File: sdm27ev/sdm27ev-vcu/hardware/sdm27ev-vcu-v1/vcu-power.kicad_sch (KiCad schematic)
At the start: 40 parts, among them IC1 TPD4E05U06QDQARQ1, IC2 TPS2121RUXR, IC3 TPS56637RPAR, IC4 TPS61023DRLT, J5 USB4725-03-C-KIT, Q1 RRL035P03FRATR, U3 HUSB238

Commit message: Minor QOL VCU edits before design review
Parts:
- added C72: 10uF, Capacitor_SMD:C_0603_1608Metric, symbol Device:C_Small
- added C73: 100nF, Capacitor_SMD:C_0603_1608Metric, symbol Device:C_Small
- added FB1: 600 Ohm 100mhz, Inductor_SMD:L_0603_1608Metric, symbol Device:FerriteBead_Small
- R32: value 20k -> 47k
- R35: now fitted
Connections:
- net 5VA: now also C72.1, C73.1, FB1.2; no longer C20.1, IC4.6 (VOUT), R12.1
- net GND: now also C72.2, C73.2
- new net: C20.1, FB1.1, IC4.6 (VOUT), R12.1
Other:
- note added: "Current limit 2.37A"
- note removed: "Current limit 1.24A"

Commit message: notes from ev vcu design review 10 3
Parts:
- added R11, R79: 5.1k, Resistor_SMD:R_0603_1608Metric, symbol Device:R_Small
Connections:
- net GND: now also R11.2, R79.2
- net at IC1.4 (D2+), J5.A5 (CC1), U3.4 (CC1): now also R79.1
- net at IC1.5 (D2-), J5.B5 (CC2), U3.5 (CC2): now also R11.1

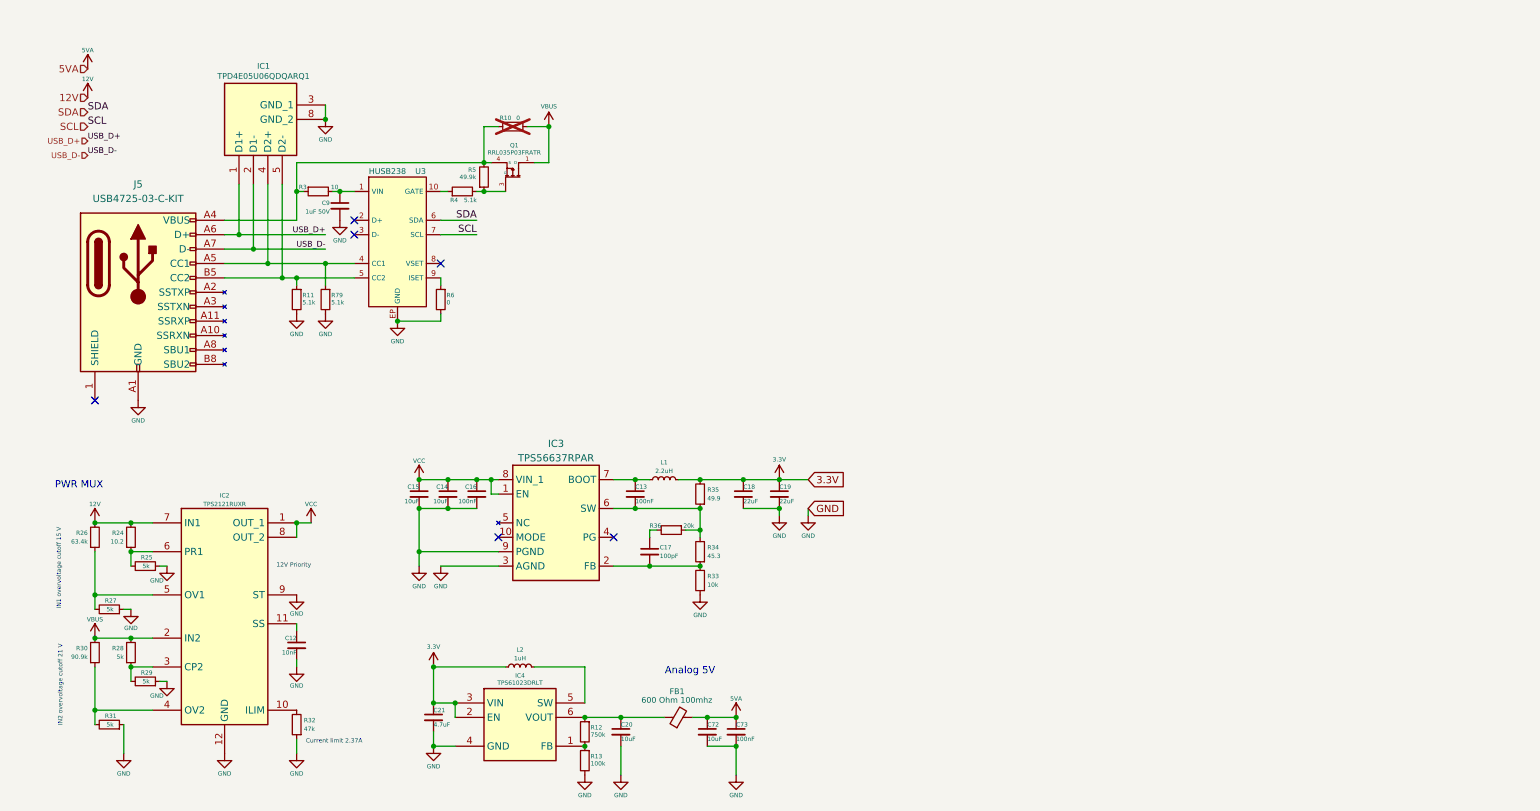
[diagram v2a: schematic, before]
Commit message: VCU sch reorg and power rework
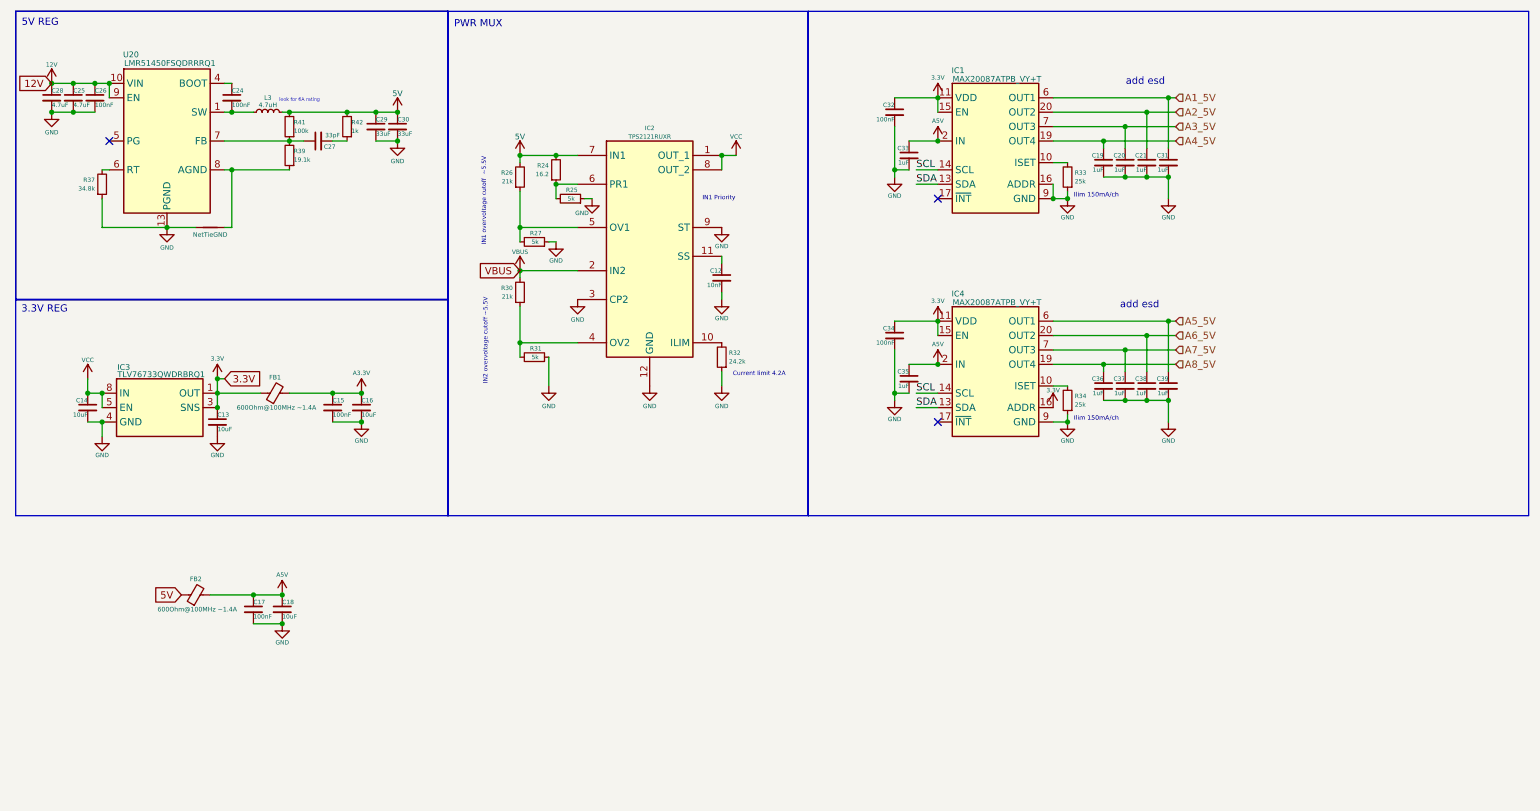
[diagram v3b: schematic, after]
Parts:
- removed C72: 10uF, Capacitor_SMD:C_0603_1608Metric, symbol Device:C_Small
- removed C73: 100nF, Capacitor_SMD:C_0603_1608Metric, symbol Device:C_Small
- removed C9: 1uF 50V, Capacitor_SMD:C_0603_1608Metric, symbol Device:C_Small
- removed IC1: TPD4E05U06QDQARQ1, DQA(R-PUSON-N10), symbol SDM_EV:TPD4E05U06QDQARQ1
- removed IC3: TPS56637RPAR, TPS56637RPAR, symbol SDM_EV:TPS56637RPAR
- removed IC4: TPS61023DRLT, SOTFL50P160X60-6N, symbol SDM_EV:TPS61023DRLT
- removed J5: USB4725-03-C-KIT, SDM_Misc:GCT_USB4730-GF-A_REVA, symbol SDM_MISC:USB4725-03-C-KIT
- removed L1: 2.2uH, Inductor_SMD:L_7.3x7.3_H3.5, symbol Device:L_Small
- removed L2: 1uH, Inductor_SMD:L_Changjiang_FTC404010S, symbol Device:L_Small
- removed Q1: RRL035P03FRATR, RRL035P03FRATR, symbol SDM_EV:RRL035P03FRATR
- removed R10, R6: 0, Resistor_SMD:R_0603_1608Metric, symbol Device:R_Small
- removed R11, R4, R79: 5.1k, Resistor_SMD:R_0603_1608Metric, symbol Device:R_Small
- removed R12: 750k, Resistor_SMD:R_0603_1608Metric, symbol Device:R_Small
- removed R13: 100k, Resistor_SMD:R_0603_1608Metric, symbol Device:R_Small
- removed R28, R29: 5k, Resistor_SMD:R_0402_1005Metric, symbol Device:R_Small
- removed R3: 10, Resistor_SMD:R_0603_1608Metric, symbol Device:R_Small
- removed R35: 49.9, Resistor_SMD:R_0402_1005Metric, symbol Device:R_Small
- removed R36: 20k, Resistor_SMD:R_0402_1005Metric, symbol Device:R_Small
- removed R5: 49.9k, Resistor_SMD:R_0603_1608Metric, symbol Device:R_Small
- removed U3: HUSB238, symbol SDM_EV:HUSB238
- added C24, C26, C32, C34: 100nF, Capacitor_SMD:C_0603_1608Metric, symbol Device:C_Small
- added C25, C28: 4.7uF, Capacitor_SMD:C_0805_2012Metric, symbol Device:C_Small
- added C27: 33pF, Capacitor_SMD:C_0603_1608Metric, symbol Device:C_Small
- added C29, C30: 33uF, Capacitor_SMD:C_0805_2012Metric, symbol Device:C_Small
- added C31, C33, C35, C36, C37, C38, C39: 1uF, Capacitor_SMD:C_0603_1608Metric, symbol Device:C_Small
- added FB2: 600Ohm@100MHz ~1.4A, Inductor_SMD:L_0805_2012Metric, symbol Device:FerriteBead_Small
- added IC1, IC4: MAX20087ATPB_VY+T, QFN50P400X400X80-21N-D, symbol SDM_EV:MAX20087ATPB_VY+T
- added IC3: TLV76733QWDRBRQ1, SON65P300X300X100-9N-D, symbol SDM_EV:TLV76733QWDRBRQ1
- added L3: 4.7uH, Inductor_SMD:L_SXN_SMDRI62, symbol Device:L_Small
- added NT1: NetTieGND, symbol Device:NetTie_2
- added R37: 34.8k, Resistor_SMD:R_0402_1005Metric, symbol Device:R_Small
- added R39: 19.1k, Resistor_SMD:R_0402_1005Metric, symbol Device:R_Small
- added R41: 100k, Resistor_SMD:R_0402_1005Metric, symbol Device:R_Small
- added R42: 1k, Resistor_SMD:R_0402_1005Metric, symbol Device:R_Small
- added U20: LMR51450FSQDRRRQ1, SON50P300X300X80-13N-D, symbol SDM_EV:LMR51450FSQDRRRQ1
- C13, C16: value 100nF -> 10uF; footprint Capacitor_SMD:C_0603_1608Metric -> Capacitor_SMD:C_0805_2012Metric
- C14: footprint Capacitor_SMD:C_0603_1608Metric -> Capacitor_SMD:C_0805_2012Metric
- C15: value 10uF -> 100nF
- C17: value 100pF -> 100nF
- C18: value 22uF -> 10uF; footprint Capacitor_SMD:C_0603_1608Metric -> Capacitor_SMD:C_0805_2012Metric
- C19: value 22uF -> 1uF
- C20: value 10uF -> 1uF
- C21: value 4.7uF -> 1uF
- FB1: value 600 Ohm 100mhz -> 600Ohm@100MHz ~1.4A; footprint Inductor_SMD:L_0603_1608Metric -> Inductor_SMD:L_0805_2012Metric
- R24: value 10.2 -> 16.2
- R26: value 63.4k -> 21k
- R30: value 90.9k -> 21k
- R32: value 47k -> 24.2k
- R33: value 10k -> 25k
- R34: value 45.3 -> 25k
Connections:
- net 12V: now also C25.1, C26.1, C28.1, U20.10 (VIN), U20.11 (VIN_2), U20.12 (VIN_3), U20.9 (EN); no longer IC2.7 (IN1), R24.2, R26.2
- net 3.3V: now also C13.1, FB1.1, C32.1, C34.1, IC1.11 (VDD), IC1.15 (EN), IC3.1 (OUT), IC3.3 (SNS), IC4.11 (VDD), IC4.15 (EN), IC4.16 (ADDR); no longer C18.1, C19.1, C21.1
- net GND: now also C13.2, C17.2, IC2.3 (CP2), R34.1, C25.2, C26.2, C28.2, C29.2, C30.2, C31.2, C32.2, C33.2, C34.2, C35.2, C36.2, C37.2, C38.2, C39.2, IC1.1 (PGND_1), IC1.12 (GND_2), IC1.16 (ADDR), IC1.21 (EP), IC1.5 (PGND_2), IC1.9 (GND), IC3.4 (GND), IC3.6 (GND_2), IC3.9 (EP), IC4.1 (PGND_1), IC4.12 (GND_2), IC4.21 (EP), IC4.5 (PGND_2), IC4.9 (GND), NT1.1, R37.1, U20.13 (PGND)
- net SCL: now also IC1.14 (SCL), IC4.14 (SCL)
- net SDA: now also IC1.13 (SDA), IC4.13 (SDA)
- net VCC: now also IC3.5 (EN), IC3.8 (IN); no longer C15.1, C16.1
- net A3_5V: now reaches C20.1
- net A3_5V: now also IC1.7 (OUT3); no longer FB1.1
- net at R34.2: now also IC4.10 (ISET); no longer C13.2
- net A5V: now reaches C17.1
- net A5V: now also C18.1, C33.1, C35.1, FB2.2, IC1.2 (IN), IC1.3 (IN_2), IC1.4 (IN_3), IC4.2 (IN), IC4.3 (IN_2), IC4.4 (IN_3)
- net 5VA renamed A3.3V
- net A3.3V: now also C15.1, C16.1
- new net: NT1.2, R39.1, U20.8 (AGND)
- new net: C27.1, R39.2, R41.1, U20.7 (FB)
- new net: C24.2, L3.1, U20.1 (SW), U20.2 (SW_2), U20.3 (SW_3)
- new net: C24.1, U20.4 (BOOT)
- new net: R37.2, U20.6 (RT)
- new net: IC1.10 (ISET), R33.2
- new net: C27.2, R42.1
- new net 5V: C29.1, C30.1, FB2.1, IC2.7 (IN1), L3.2, R24.2, R26.2, R41.2, R42.2
- new net A1_5V: C31.1, IC1.6 (OUT1)
- new net A2_5V: C21.1, IC1.20 (OUT2)
- new net A4_5V: C19.1, IC1.19 (OUT4)
- new net A5_5V: C39.1, IC4.6 (OUT1)
- new net A6_5V: C38.1, IC4.20 (OUT2)
- new net A7_5V: C37.1, IC4.7 (OUT3)
- new net A8_5V: C36.1, IC4.19 (OUT4)
- no-connect marks 6 -> 3
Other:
- note added: "3.3V REG"
- note added: "5V REG"
- note added: "Current limit 4.2A"
- note added: "IN1 Priority"
- note added: "IN1 overvoltage cutoff ~5.5V"
- note added: "IN2 overvoltage cutoff ~5.5V"
- note added: "Ilim 150mA/ch"
- note added: "add esd"
- note added: "look for 6A rating"
- note removed: "12V Priority"
- note removed: "Analog 5V"
- note removed: "Current limit 2.37A"
- note removed: "IN1 overvoltage cutoff 15 V"
- note removed: "IN2 overvoltage cutoff 21 V"
- moved on the sheet: C12, IC2, R24, R25, R26, R27, R30, R31, R32

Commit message: EV VCU edits, mostly organizational and pre layout/footprint assigned
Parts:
- IC1, IC4: footprint QFN50P400X400X80-21N-D -> SDM_EV:QFN50P400X400X80-21N-D
- IC3: footprint SON65P300X300X100-9N-D -> (none)
- R24, R25, R26, R27, R30, R31, R32, R33, R34, R37, R39, R41, R42: footprint Resistor_SMD:R_0402_1005Metric -> Resistor_SMD:R_0603_1608Metric
- U20: footprint SON50P300X300X80-13N-D -> SDM_EV:SON50P300X300X80-13N-D
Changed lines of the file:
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@@
 	)
 	(junction
-		(at 73.66 80.01)
-		(diameter 0)
-		(color 0 0 0 0)
-	)
-	(junction
 		(at 175.26 74.93)
 		(diameter 0)
@@
 	)
 	(junction
+		(at 73.66 77.47)
+		(diameter 0)
+		(color 0 0 0 0)
+	)
+	(junction
 		(at 167.64 40.64)
 		(diameter 0)
@@
 	)
 	(junction
+		(at 73.66 80.01)
+		(diameter 0)
+		(color 0 0 0 0)
+	)
+	(junction
 		(at 39.37 50.8)
 		(diameter 0)
@@
 	(wire
 		(pts
+			(xy 73.66 77.47) (xy 74.93 77.47)
+		)
+		(stroke
+			(width 0)
+			(type default)
+		)
+	)
+	(wire
+		(pts
 			(xy 167.64 80.01) (xy 170.18 80.01)
 		)
@@
 	(wire
 		(pts
+			(xy 73.66 77.47) (xy 73.66 80.01)
+		)
+		(stroke
+			(width 0)
+			(type default)
+		)
+	)
+	(wire
+		(pts
 			(xy 19.05 30.48) (xy 22.86 30.48)
 		)
@@
 		)
 	)
+	(global_label "A3.3V"
+		(shape input)
+		(at 74.93 77.47 0)
+		(fields_autoplaced yes)
+		(effects
+			(font
+				(size 1.27 1.27)
+			)
+			(justify left)
+		)
+		(property "Intersheetrefs" "${INTERSHEET_REFS}"
+			(at 83.1162 77.47 0)
+			(hide yes)
+			(show_name no)
+			(do_not_autoplace no)
+			(effects
+				(font
+					(size 1.27 1.27)
+				)
+				(justify left)
+			)
+		)
+	)
 	(global_label "12V"
 		(shape input)
@@
 		)
 	)
+	(global_label "VCC"
+		(shape input)
+		(at 139.7 38.1 0)
+		(fields_autoplaced yes)
+		(effects
+			(font
+				(size 1.27 1.27)
+			)
+			(justify left)
+		)
+		(property "Intersheetrefs" "${INTERSHEET_REFS}"
+			(at 146.3138 38.1 0)
+			(hide yes)
+			(show_name no)
+			(do_not_autoplace no)
+			(effects
+				(font
+					(size 1.27 1.27)
+				)
+				(justify left)
+			)
+		)
+	)
 	(hierarchical_label "A8_5V"
 		(shape input)
@@
 			)
 		)
-		(property "Footprint" "SON65P300X300X100-9N-D"
+		(property "Footprint" ""
 			(at 52.07 174.93 0)
 			(hide yes)
@@
 			)
 		)
-		(property "Footprint" "Resistor_SMD:R_0402_1005Metric"
+		(property "Footprint" "Resistor_SMD:R_0603_1608Metric"
 			(at 137.16 73.66 0)
 			(hide yes)
@@
 			)
 		)
-		(property "Footprint" "Resistor_SMD:R_0402_1005Metric"
+		(property "Footprint" "Resistor_SMD:R_0603_1608Metric"
 			(at 60.96 38.1 0)
 			(hide yes)
@@
 			)
 		)
-		(property "Footprint" "SON50P300X300X80-13N-D"
+		(property "Footprint" "SDM_EV:SON50P300X300X80-13N-D"
 			(at 53.34 120.32 0)
 			(hide yes)
@@
 			)
 		)
-		(property "Footprint" "Resistor_SMD:R_0402_1005Metric"
+		(property "Footprint" "Resistor_SMD:R_0603_1608Metric"
 			(at 60.96 33.02 0)
 			(hide yes)
@@
 	(symbol
 		(lib_id "power:+3.3V")
-		(at 73.66 80.01 0)
+		(at 73.66 77.47 0)
 		(unit 1)
 		(body_style 1)
@@
 		(dnp no)
 		(property "Reference" "#PWR0161"
-			(at 73.66 83.82 0)
+			(at 73.66 81.28 0)
 			(hide yes)
 			(show_name no)
@@
 		)
 		(property "Value" "A3.3V"
-			(at 73.66 76.454 0)
+			(at 73.66 73.914 0)
 			(show_name no)
 			(do_not_autoplace no)
@@
 		)
 		(property "Footprint" ""
-			(at 73.66 80.01 0)
+			(at 73.66 77.47 0)
 			(hide yes)
 			(show_name no)
@@
 		)
 		(property "Datasheet" ""
-			(at 73.66 80.01 0)
+			(at 73.66 77.47 0)
 			(hide yes)
 			(show_name no)
@@
 		)
 		(property "Description" "Power symbol creates a global label with name \"+3.3V\""
-			(at 73.66 80.01 0)
+			(at 73.66 77.47 0)
 			(hide yes)
 			(show_name no)
@@
 			)
 		)
-		(property "Footprint" "Resistor_SMD:R_0402_1005Metric"
+		(property "Footprint" "Resistor_SMD:R_0603_1608Metric"
 			(at 198.12 41.91 0)
 			(hide yes)
@@
 			)
 		)
-		(property "Footprint" "Resistor_SMD:R_0402_1005Metric"
+		(property "Footprint" "Resistor_SMD:R_0603_1608Metric"
 			(at 104.14 53.34 0)
 			(hide yes)
@@
 			)
 		)
-		(property "Footprint" "Resistor_SMD:R_0402_1005Metric"
+		(property "Footprint" "Resistor_SMD:R_0603_1608Metric"
 			(at 104.14 73.66 0)
 			(hide yes)
@@
 			)
 		)
-		(property "Footprint" "Resistor_SMD:R_0402_1005Metric"
+		(property "Footprint" "Resistor_SMD:R_0603_1608Metric"
 			(at 198.12 81.28 0)
 			(hide yes)
@@
 			)
 		)
-		(property "Footprint" "QFN50P400X400X80-21N-D"
+		(property "Footprint" "SDM_EV:QFN50P400X400X80-21N-D"
 			(at 201.93 122.86 0)
 			(hide yes)
@@
 			)
 		)
-		(property "Footprint" "Resistor_SMD:R_0402_1005Metric"
+		(property "Footprint" "Resistor_SMD:R_0603_1608Metric"
 			(at 71.12 33.02 0)
 			(hide yes)
@@
 			)
 		)
-		(property "Footprint" "Resistor_SMD:R_0402_1005Metric"
+		(property "Footprint" "Resistor_SMD:R_0603_1608Metric"
 			(at 110.49 45.72 0)
 			(hide yes)
@@
 			)
 		)
-		(property "Footprint" "QFN50P400X400X80-21N-D"
+		(property "Footprint" "SDM_EV:QFN50P400X400X80-21N-D"
 			(at 201.93 162.23 0)
 			(hide yes)
@@
 			)
 		)
-		(property "Footprint" "Resistor_SMD:R_0402_1005Metric"
+		(property "Footprint" "Resistor_SMD:R_0603_1608Metric"
 			(at 101.6 62.23 0)
 			(hide yes)
@@
 			)
 		)
-		(property "Footprint" "Resistor_SMD:R_0402_1005Metric"
+		(property "Footprint" "Resistor_SMD:R_0603_1608Metric"
 			(at 101.6 41.91 0)
 			(hide yes)
@@
 			)
 		)
-		(property "Footprint" "Resistor_SMD:R_0402_1005Metric"
+		(property "Footprint" "Resistor_SMD:R_0603_1608Metric"
 			(at 27.94 43.18 0)
 			(hide yes)
@@
 			)
 		)
-		(property "Footprint" "Resistor_SMD:R_0402_1005Metric"
+		(property "Footprint" "Resistor_SMD:R_0603_1608Metric"
 			(at 107.95 40.64 0)
 			(hide yes)
